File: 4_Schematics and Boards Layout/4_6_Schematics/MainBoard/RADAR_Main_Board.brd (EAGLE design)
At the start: 260 x 300 mm, 825 parts, among them IC1 AT93C46A-10SQ-2.7, J1 142-0731-211, J18 142-0731-211, J19 CJT-T-P-HH-ST-TH1, J20 142-0731-211, J21 CJT-T-P-HH-ST-TH1, J22 142-0731-211, J23 142-0731-211, J24 142-0731-211, J25 142-0731-211, J26 142-0731-211, J27 142-0731-211, J28 142-0731-211, J29 142-0731-211, J30 142-0731-211, J31 142-0731-211, J32 142-0731-211, J33 142-0731-211, J34 142-0731-211, J35 142-0731-211, J36 142-0731-211, J37 142-0731-211, J38 142-0731-211, J39 142-0731-211, J40 142-0731-211, J41 142-0731-211, J42 142-0731-211, J43 142-0731-211, J44 142-0731-211, J45 142-0731-211, J46 142-0731-211, J47 142-0731-211, J48 142-0731-211, J49 142-0731-211, J50 142-0731-211, J51 142-0731-211, J52 142-0731-211, J53 142-0731-211, J54 142-0731-211, J55 142-0731-211, J56 142-0731-211, J57 142-0731-211, J58 142-0731-211, J59 142-0731-211, U1 AD9484BCPZ-500, U10 ADS7830IPWR, U11 INA241A4IDGKRDGK0008A-MFG, U13 LTC5552IUDBTRMPBF, U14 SZMMSZ5232BT1G, U15 SZMMSZ5232BT1G, U16 EP4RKU+, U17 SZMMSZ5232BT1G, U2 STM32F746ZGT7, U3 AD9708AR, U37 SZMMSZ5232BT1G, U38 SZMMSZ5232BT1G, U39 SZMMSZ5232BT1G, U4 AD8352ACPZ-R7, U40 SZMMSZ5232BT1G, U41 SZMMSZ5232BT1G, U42 XC7A50T-2FTG256I, U43 SZMMSZ5232BT1G, U44 SZMMSZ5232BT1G, U45 SZMMSZ5232BT1G, U46 SZMMSZ5232BT1G, U47 SZMMSZ5232BT1G, U48 SZMMSZ5232BT1G, U49 SZMMSZ5232BT1G, U5 LTC5552IUDBTRMPBF, U50 SZMMSZ5232BT1G, U51 SZMMSZ5232BT1G, U52 SZMMSZ5232BT1G, U53 SZMMSZ5232BT1G, U54 SZMMSZ5232BT1G, U55 SZMMSZ5232BT1G, U56 SZMMSZ5232BT1G, U57 SZMMSZ5232BT1G, U58 SZMMSZ5232BT1G, U59 SZMMSZ5232BT1G, U6 FT2232HQ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

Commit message: feat(hw): a working AD9484 serial port, and the part-number sweep (#14 #22)
#14 the AD9484's serial port could not be used at all
  CSB was tied to a supply rail - the datasheet names that as the way to disable the SPI -
  SCLK/DFS was decided by solder jumper SJ1, and SDIO was not connected.  The pins are
  DRVDD-referenced 1.8 V logic: the absolute maximum is "SDIO/DCS to DRGND: -0.3 V to
  DRVDD + 0.2 V", i.e. 2.0 V, and the equivalent input circuits show CSB and SDIO referenced to
  DRVDD.  They cannot be driven from a 3.3 V bank, and the FPGA's 1.8 V bank has one free pin,
  so a translator is required - and the repo already had the part, U90/U91 from the flash work.

  U92 (TXS0104EPWR) sits between the ADC and the MCU: VCCA on the ADC's own digital supply,
  VCCB on +3V3, OE pulled up to VCCA, and the three signals on PC10/PC11/PC13.  The master is
  the MCU rather than the FPGA - all three parts are on the main board, the MCU owns bring-up,
  and the port is slow (tCLK >= 40 ns), so bit-banging is ample and no RTL is needed.

  Two deliberate choices, both safe at power-up: SCLK/DFS idles LOW, because the datasheet's
  default is offset binary and nothing in the FPGA converts two's complement - SJ1 as built
  strapped it to a 1.8 V rail, i.e. two's complement, which would put the whole capture half a
  scale out; and CSB idles HIGH through the translator's internal pull-up, so the ADC stays in
  strapped mode until the firmware talks.

  AD9484_SPI.{h,c} implement the 16-bit instruction + 8-bit data frame from the datasheet's
  serial timing, with readback turnaround, and use the registers the memory map names: 0x0D
  TEST_IO, 0x14 OUTPUT_MODE (00 = offset binary, 01 = two's complement), 0x19/0x1A user
  pattern.  Bring-up selects offset binary explicitly rather than trusting the strap, reads
  back 0x2A (OVR_CONFIG, default 0x01) and reports both, so a dead interface shows as a wrong
  value in telemetry instead of as a silently missing feature.

#22 the pa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
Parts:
- added R194: 10k, rcl:R0201
- added R195: 4.7k, rcl:R0201
- added U92: TXS0104EPWR, My_Library_RADAR:PW0014A-MFG
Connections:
- new net ADC_SPI_CSB: U1.27, U92.A1
- new net ADC_SPI_SCLK: R195.1, SJ1.2, U1.26, U92.A2
- new net ADC_SPI_SDIO: U1.25, U92.A3
- new net MCU_ADC_CSB: U2.111, U92.B1
- new net MCU_ADC_SCLK: U2.112, U92.B2
- new net MCU_ADC_SDIO: U2.7, U92.B3
- new net N$U92_OE: R194.1, U92.OE
- net +1V8_CLOCK_F: no longer U1.27
- net +1V8_FPGA: now also R194.2, U92.VCCA
- net +3V3: now also U92.VCCB
- net GND: now also R195.2, SJ1.3, U92.GND
- net N$6: no longer U1.26

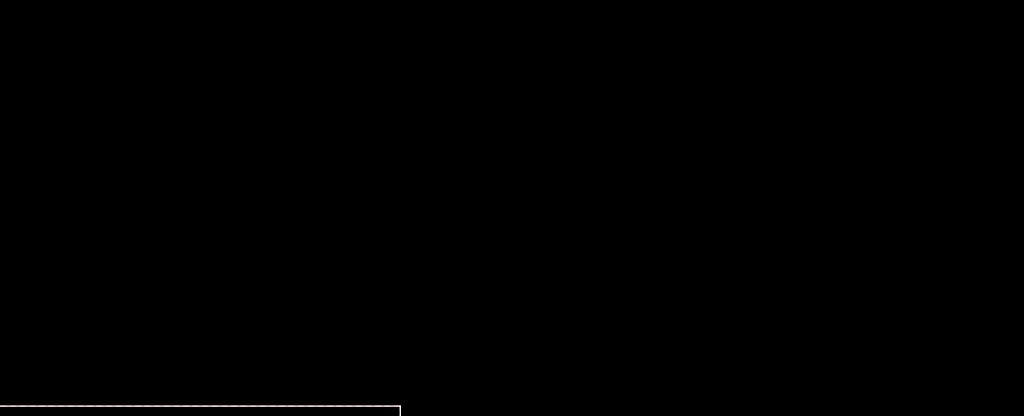
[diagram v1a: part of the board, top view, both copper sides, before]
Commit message: feat(hw): the eight temperature channels, and a filter that meets the requirement (#5 #7)
#5 The issue said the harness had no spare position, so the sensors could not reach the MCU. The
   second half was the wrong question: the main board already carries the whole interface.

   Three ADS7830s exist and are in the BOM - U10 (0x48), U88 (0x4A), U89 (0x4B) - and the firmware
   names exactly these hadc1/hadc2/hadc3. U89's eight channels run to eight 3-pin headers (JP5,
   JP6, JP11, JP12, JP14, JP15, JP16, JP19), each bringing out +3V3_AN4_F, the channel and GND.
   The probes are therefore external, on flying leads, and belong at the PA where the temperature
   is actually wanted.

   What was missing was three things:
     * a pull-up - the channel nets carried only the header and the ADC pin, so an NTC would have
       had nothing to divide against.  Eight 10k 0201 resistors (R196-R203) now pull each channel
       up to +3V3_AN4_F, reusing the repo's own rcl/R-EU_/R0201 deviceset;
     * names - the anonymous N$ nets are now TEMP_1..TEMP_8 in U89's channel order, so the
       firmware's index maps onto the net name;
     * a firmware bug - hadc3 was read eight times per cycle and NEVER INITIALISED.  Only hadc1
       and hadc2 were.  Every Temperature_N was reading an unconfigured part.

   The conversion was wrong in two different ways as well: the bring-up read stored raw 8-bit
   codes while the loop read applied a linear *0.64705f, and neither is right for a thermistor.
   Both sites now call one reader using PA_Thermal_NtcToCelsius(), which inverts the divider and
   applies the B-equation, and returns false for an unplugged probe - which sits on the rail and
   would otherwise read as a very cold board.

   The model reproduces the design's own numbers: with a 10k pull-up equal to the probe's R25 the
   divider midpoint is exactly 25.0 degC, and ratio 0.10 lands on 95.3 degC, which is the case
   limit derived from the QPA2962's theta_JC (95.4 degC).  Th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
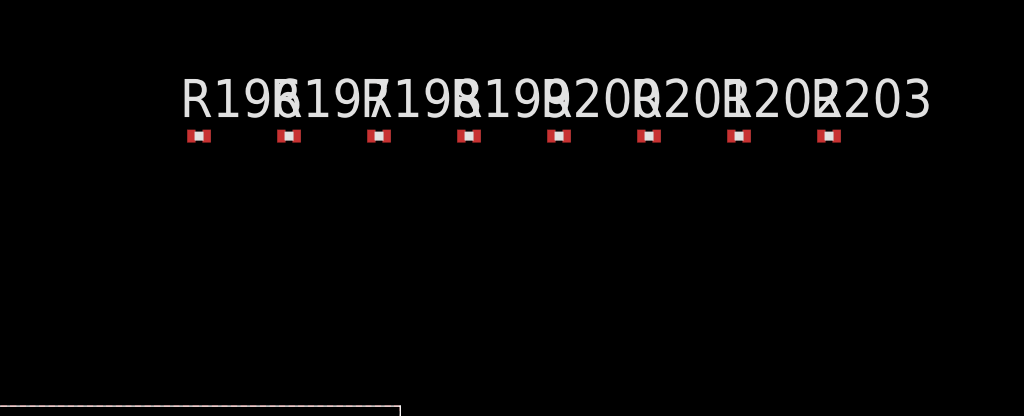
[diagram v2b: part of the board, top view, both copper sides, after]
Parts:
- added R196, R197, R198, R199, R200, R201, R202, R203: 10k, rcl:R0201
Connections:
- removed net N$295: JP5.2, U89.4
- removed net N$296: JP6.2, U89.5
- removed net N$297: JP19.2, U89.1
- removed net N$298: JP12.2, U89.7
- removed net N$299: JP14.2, U89.2
- removed net N$301: JP16.2, U89.8
- removed net N$306: JP11.2, U89.6
- removed net N$307: JP15.2, U89.3
- new net TEMP_1: JP19.2, R196.1, U89.1
- new net TEMP_2: JP14.2, R197.1, U89.2
- new net TEMP_3: JP15.2, R198.1, U89.3
- new net TEMP_4: JP5.2, R199.1, U89.4
- new net TEMP_5: JP6.2, R200.1, U89.5
- new net TEMP_6: JP11.2, R201.1, U89.6
- new net TEMP_7: JP12.2, R202.1, U89.7
- new net TEMP_8: JP16.2, R203.1, U89.8
- net +3V3_AN4_F: now also R196.2, R197.2, R198.2, R199.2, R200.2, R201.2, R202.2, R203.2
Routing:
- net TEMP_8: track 0.00 -> 35.2 mm
- net N$301: track 35.2 -> 0.00 mm
- net TEMP_1: track 0.00 -> 25.6 mm
- net N$297: track 25.6 -> 0.00 mm
- net TEMP_7: track 0.00 -> 25.5 mm
- net N$298: track 25.5 -> 0.00 mm
- net TEMP_2: track 0.00 -> 22.7 mm
- net N$299: track 22.7 -> 0.00 mm
- net TEMP_6: track 0.00 -> 20.8 mm
- net N$306: track 20.8 -> 0.00 mm
- net TEMP_3: track 0.00 -> 17.3 mm
- net N$307: track 17.3 -> 0.00 mm
- net TEMP_5: track 0.00 -> 15.9 mm
- net N$296: track 15.9 -> 0.00 mm
- net TEMP_4: track 0.00 -> 13.8 mm
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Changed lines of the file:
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@@
 <attribute name="SPICEPREFIX" value="C" x="53.7469375" y="136.535715625" size="1.778" layer="27" rot="R180" display="off"/>
 </element>
-</elements>
+    <element name="R196" library="rcl" deviceset="R-EU_" device="R0201" package="R0201" value="10k" x="253.292" y="309.000"/>
+    <element name="R197" library="rcl" deviceset="R-EU_" device="R0201" package="R0201" value="10k" x="256.292" y="309.000"/>
+    <element name="R198" library="rcl" deviceset="R-EU_" device="R0201" package="R0201" value="10k" x="259.292" y="309.000"/>
+    <element name="R199" library="rcl" deviceset="R-EU_" device="R0201" package="R0201" value="10k" x="262.292" y="309.000"/>
+    <element name="R200" library="rcl" deviceset="R-EU_" device="R0201" package="R0201" value="10k" x="265.292" y="309.000"/>
+    <element name="R201" library="rcl" deviceset="R-EU_" device="R0201" package="R0201" value="10k" x="268.292" y="309.000"/>
+    <element name="R202" library="rcl" deviceset="R-EU_" device="R0201" package="R0201" value="10k" x="271.292" y="309.000"/>
+    <element name="R203" library="rcl" deviceset="R-EU_" device="R0201" package="R0201" value="10k" x="274.292" y="309.000"/></elements>
 <signals><signal name="MCU_ADC_SDIO" class="0"><contactref element="U92" pad="B3"/><contactref element="U2" pad="7"/></signal><signal name="MCU_ADC_SCLK" class="0"><contactref element="U92" pad="B2"/><contactref element="U2" pad="112"/></signal><signal name="MCU_ADC_CSB" class="0"><contactref element="U92" pad="B1"/><contactref element="U2" pad="111"/></signal><signal name="ADC_SPI_SDIO" class="0"><contactref element="U1" pad="25"/><contactref element="U92" pad="A3"/></signal><signal name="ADC_SPI_SCLK" class="0"><contactref element="U1" pad="26"/><contactref element="U92" pad="A2"/><contactref element="R195" pad="1"/><contactref element="SJ1" pad="2"/></signal><signal name="ADC_SPI_CSB" class="0"><contactref element="U1" pad="27"/><contactref element="U92" pad="A1"/></signal><signal name="N$U92_OE" class="0"><contactref element="U92" pad="OE"/><contactref element="R194" pad="1"/></signal><signal name="FPGA_STROBE_ACK" class="0"><contactref element="U42" pad="B16"/><contactref element="U2" pad="29"/></signal><signal name="PG_2V5_FPGA" class="0"><contactref element="X27" pad="1"/><contactref element="U2" pad="28"/></signal><signal name="PG_3V3_XO" class="0"><contactref element="X26" pad="1"/><contactref element="U2" pad="27"/></signal><signal name="PG_3V3_ADTR" class="0"><contactref element="X25" pad="1"/><contactref element="U2" pad="26"/></signal><signal name="N$U91_OE" class="0"><contactref element="U91" pad="6"/><contactref element="R177" pad="1"/></signal><signal name="N$U90_OE" class="0"><contactref element="U90" pad="8"/><contactref element="R176" pad="1"/></signal><signal name="+2V5_FPGA" class="0"><contactref element="U90" pad="1"/><contactref element="U91" pad="3"/><contactref element="R176" pad="2"/><contactref element="R177" pad="2"/><contactref element="C354" pad="1"/><contactref element="C355" pad="1"/><contactref element="C358" pad="1"/><contactref element="C359" pad="1"/><contactref element="X57" pad="1"/><contactref element="U42" pad="L16"/><contactref element="U42" pad="M13"/><contactref element="U42" pad="N10"/><contactref element="U42" pad="P7"/><contactref element="U42" pad="R14"/><contactref element="U42" pad="T11"/></signal><signal name="FLASH_NRST_F" class="0"><contactref element="U9" pad="A4"/><contactref element="U91" pad="1"/></signal><signal name="FLASH_NCS_F" class="0"><contactref element="U9" pad="C2"/><contactref element="U91" pad="8"/></signal><signal name="FLASH_DQ3_F" class="0"><contactref element="U9" pad="D4"/><contactref element="U90" pad="10"/></signal><signal name="FLASH_DQ2_F" class="0"><contactref element="U9" pad="C4"/><contactref element="U90" pad="11"/></signal><signal name="FLASH_DQ1_F" class="0"><contactref element="U9" pad="D2"/><contactref element="U90" pad="12"/></signal><signal name="FLASH_DQ0_F" class="0"><contactref element="U9" pad="D3"/><contactref element="U90" pad="13"/></signal>
 <signal name="+3V3">
@@
 <wire x1="196.5" y1="33" x2="196.5" y2="52.5" width="0.1" layer="16"/>
 <wire x1="196.5" y1="33" x2="196.35" y2="32.95" width="0.1" layer="16"/>
-</signal>
+        <contactref element="R196" pad="2"/>
+        <contactref element="R197" pad="2"/>
+        <contactref element="R198" pad="2"/>
+        <contactref element="R199" pad="2"/>
+        <contactref element="R200" pad="2"/>
+        <contactref element="R201" pad="2"/>
+        <contactref element="R202" pad="2"/>
+        <contactref element="R203" pad="2"/></signal>
 <signal name="+3V3_AN5_F">
 <contactref element="L21" pad="2"/>
@@
 <wire x1="200.275" y1="30.79" x2="200.33" y2="30.735" width="0.2" layer="1"/>
 </signal>
-<signal name="N$295">
+<signal name="TEMP_4">
 <contactref element="JP5" pad="2"/>
 <contactref element="U89" pad="4"/>
@@
 <wire x1="200.925" y1="47.297" x2="203.608" y2="49.98" width="0.203996875" layer="1"/>
 <wire x1="203.608" y1="49.98" x2="204.37" y2="49.98" width="0.203996875" layer="1"/>
-</signal>
-<signal name="N$296">
+        <contactref element="R199" pad="1"/></signal>
+<signal name="TEMP_5">
 <contactref element="U89" pad="5"/>
 <contactref element="JP6" pad="2"/>
@@
 <wire x1="200.275003125" y1="41.474996875" x2="200.275003125" y2="38.0794" width="0.204" layer="1"/>
 <wire x1="196.2" y1="45.55" x2="200.275003125" y2="41.474996875" width="0.204" layer="1"/>
-</signal>
-<signal name="N$298">
+        <contactref element="R200" pad="1"/></signal>
+<signal name="TEMP_7">
 <contactref element="JP12" pad="2"/>
 <contactref element="U89" pad="7"/>
@@
 <wire x1="199" y1="39.5" x2="199" y2="38.104396875" width="0.204" layer="1"/>
 <wire x1="199" y1="38.104396875" x2="198.975003125" y2="38.0794" width="0.204" layer="1"/>
-</signal>
-<signal name="N$301">
+        <contactref element="R202" pad="1"/></signal>
+<signal name="TEMP_8">
 <contactref element="JP16" pad="2"/>
 <contactref element="U89" pad="8"/>
@@
 <wire x1="181.0206" y1="38.0794" x2="198.325" y2="38.0794" width="0.204" layer="1"/>
 <wire x1="177.35" y1="41.75" x2="181.0206" y2="38.0794" width="0.204" layer="1"/>
-</signal>
-<signal name="N$306">
+        <contactref element="R203" pad="1"/></signal>
+<signal name="TEMP_6">
 <contactref element="JP11" pad="2"/>
 <contactref element="U89" pad="6"/>
@@
 <wire x1="199.625" y1="40.875" x2="199.625" y2="38.0794" width="0.204" layer="1"/>
 <wire x1="191.1" y1="44" x2="192.9" y2="42.2" width="0.204" layer="1"/>
-</signal>
-<signal name="N$307">
+        <contactref element="R201" pad="1"/></signal>
+<signal name="TEMP_3">
 <contactref element="JP15" pad="2"/>
 <contactref element="U89" pad="3"/>
@@
 <wire x1="207.698" y1="45.498" x2="207.698" y2="45.578265625" width="0.204" layer="1"/>
 <wire x1="201.575" y1="42.025" x2="203.85" y2="44.3" width="0.204" layer="1"/>
-</signal>
-<signal name="N$299">
+        <contactref element="R198" pad="1"/></signal>
+<signal name="TEMP_2">
 <contactref element="U89" pad="2"/>
 <contactref element="JP14" pad="2"/>
@@
 <wire x1="213.93" y1="50.13" x2="214.92" y2="50.13" width="0.204" layer="1"/>
 <wire x1="202.225" y1="41.075" x2="204.35" y2="43.2" width="0.204" layer="1"/>
-</signal>
-<signal name="N$297">
+        <contactref element="R197" pad="1"/></signal>
+<signal name="TEMP_1">
 <contactref element="JP19" pad="2"/>
 <contactref element="U89" pad="1"/>
@@
 <wire x1="215.3" y1="42.05" x2="205" y2="42.05" width="0.204" layer="1"/>
 <wire x1="205" y1="42.05" x2="202.875" y2="39.925" width="0.204" layer="1"/>
-</signal>
+        <contactref element="R196" pad="1"/></signal>
 <signal name="N$207">
 <contactref element="X3" pad="1"/>

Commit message: fix(bom): correct five Yageo value codes to their E96 forms (#22)
The errata found that RC0201FR / RC0402FR are Yageo's 1% (F) = E96 series and that none of the five
values in the BOM is an E96 code - while the nearest E96 value resolves at a distributor in every case
and the BOM's form resolves nowhere.  This applies the correction.

  2.443k / RC0201FR-072K44L  ->  2.43k  / RC0201FR-072K43L    (26 designators)
  3k2    / RC0201FR-073K2L   ->  3.16k  / RC0201FR-073K16L   (R33)
  500R   / RC0201FR-07500RL  ->  499R   / RC0201FR-07499RL   (R110, R112-R114)
  840R   / RC0201FR-07840RL  ->  845R   / RC0201FR-07845RL   (R78-R81)
  830R   / RC0402FR-07830RL  ->  825R   / RC0402FR-07825RL   (R36)

Applied in all three places that have to agree - the schematic part's value, the board element's
value, and the BOM row's Value and MPN - because the BOM gate compares the board's value against the
sheet's, and a half-applied change is exactly the defect that check exists to catch.  Each BOM row
carries the reason in its remark column so the change is auditable rather than silent.

Why this is safe: every substitution is smaller than the 1% tolerance the parts already carry
(-0.5%, -1.25%, -0.2%, +0.6%, -0.6%), and all instances of each part number change together, so any
matched set keeps its ratio.

Effect: the five corrected part numbers resolve, so the orderability count moves from 171 to 176 of
179 rows.  The three remaining are the Murata parts whose series is confirmed but whose individual
pages did not surface - a search limit rather than a BOM defect.

The gate caught the change as intended: bom_orderability failed immediately after the edit because
the new part numbers were not yet in the verified list, which is the check doing its job.

Full CI sweep on the pinned interpreter: ruff clean; eight gates green; make test 7/7, 51/51, 36/36;
unit tests 171 passed 3 skipped; cross-layer 45 passed; FPGA regression 32/32.
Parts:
- R103, R104, R105, R106, R119, R120, R121, R122, R89, R90, R91, R92, R95, R96, R97, R98: value 2.443k -> 2.43k
- R110, R112, R113, R114: value 500R -> 499R
- R33: value 3k2 -> 3.16k
- R36: value 830R -> 825R
- R78, R79, R80, R81: value 840R -> 845R
